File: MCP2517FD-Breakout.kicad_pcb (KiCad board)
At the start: 2 copper layers, 40.6 x 21.6 mm, 17 parts, among them J1 Conn_01x07_Male, J2 Conn_01x04_Male, U1 MCP2517FD-xSL, U2 AMS1117-3.3, U3 MCP2562-E-SN, Y1 Crystal

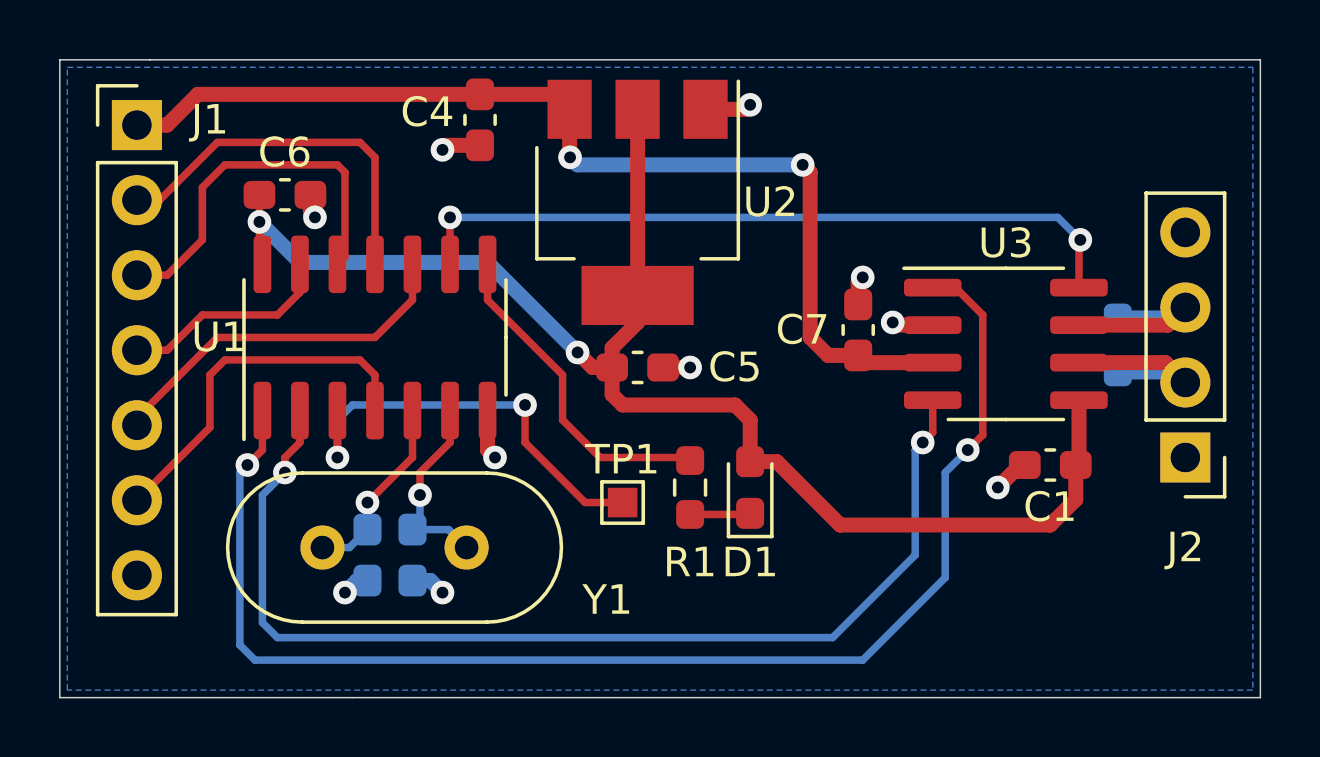
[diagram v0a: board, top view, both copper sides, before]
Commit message: update pcb, optime can tx rx routing
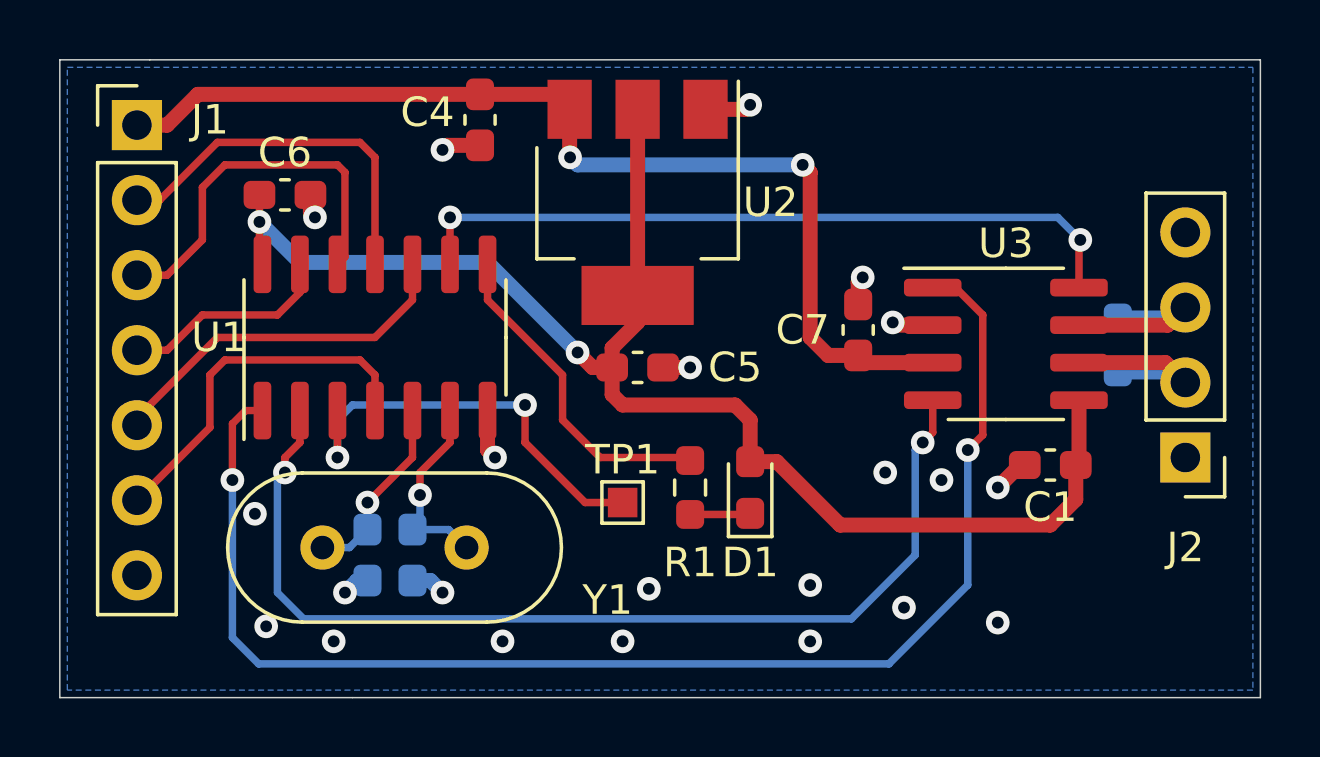
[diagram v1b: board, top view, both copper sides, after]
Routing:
- net /RXCAN: track 36.7 -> 34.8 mm
- net /TXCAN: track 45.0 -> 46.2 mm
- net GND: vias 10 -> 22
